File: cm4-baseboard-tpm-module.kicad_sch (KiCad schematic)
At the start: 37 parts, among them J1 Plug_Samtec_ERM5_2x20_ERM5-02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, U1 SLB9672XU20FW1624XTMA1

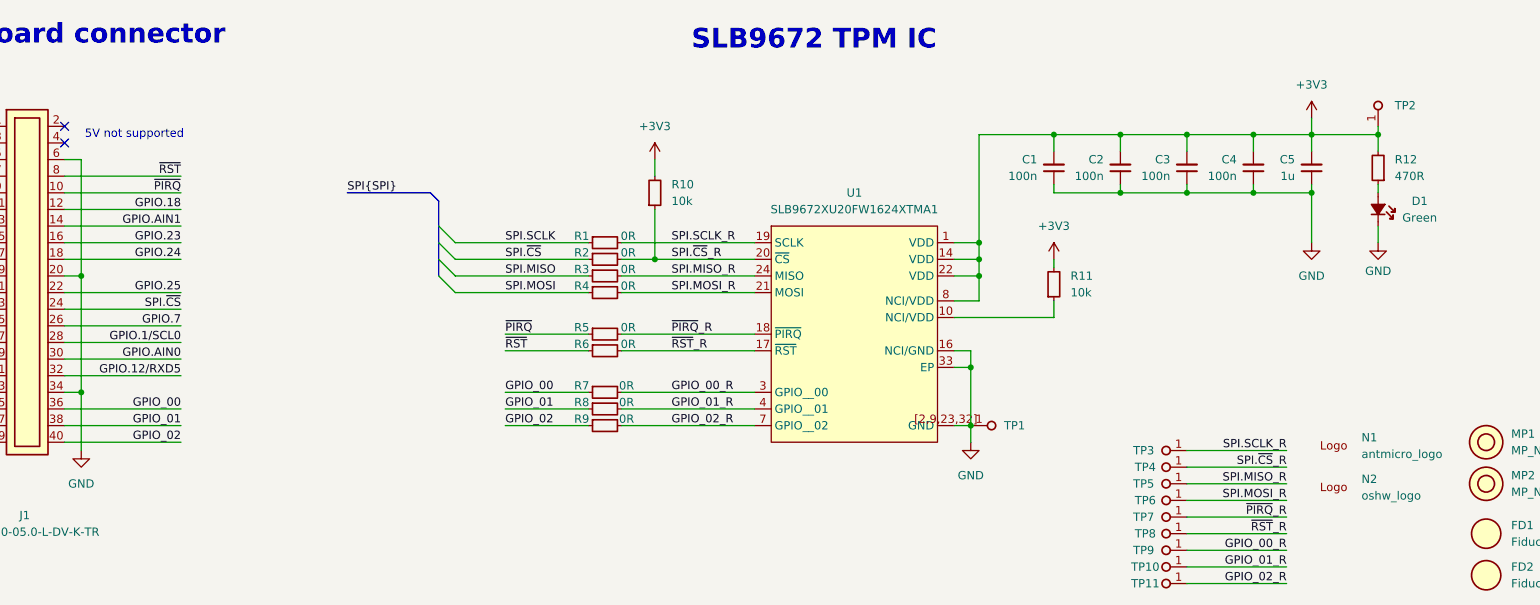
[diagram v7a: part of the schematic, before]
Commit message: [#104798] Create 2-layer board version
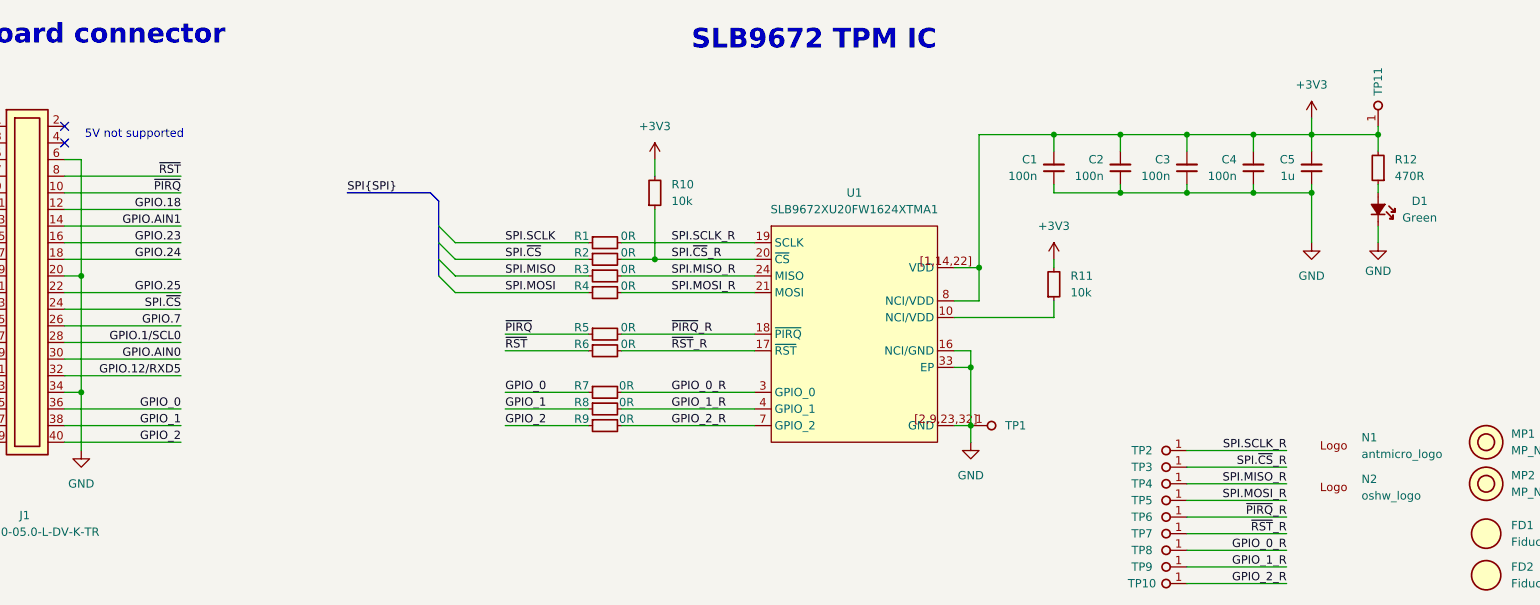
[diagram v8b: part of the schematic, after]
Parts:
- removed TP1, TP10, TP11, TP2, TP3, TP4, TP5, TP6, TP7, TP8, TP9: TP_Pad0.75mm_Drill0.2mm, antmicro-footprints:TP_Pad0.75mm_Drill0.2mm, symbol antmicroTestPoints:TP_Pad0.75mm_Drill0.2mm
- added TP1, TP10, TP11, TP2, TP3, TP4, TP5, TP6, TP7, TP8, TP9: TP_0.75mm_SMD, antmicro-footprints:TP_SMD_0.75mm, symbol antmicroTestPoints:TP_0.75mm_SMD
- U1: footprint antmicro-footprints:QFN-32-1EP_5x5mm_P0.5mm -> antmicro-footprints:UQFN-32-1EP_5x5mm_P0.5mm_EP3.6x3.6mm; License (none) -> Apache-2.0
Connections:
- net +3V3: now also U1.[1,14,22] (VDD), TP11.1; no longer U1.1 (VDD), U1.14 (VDD), U1.22 (VDD)
- net GND: now also TP1.1
- net SPI.MISO_R: now also TP4.1
- net SPI.MOSI_R: now also TP5.1
- net SPI.SCLK_R: now also TP2.1
- net SPI.~{CS}_R: now also TP3.1
- net ~{PIRQ}_R: now also TP6.1
- net ~{RST}_R: now also TP7.1
- net GPIO_00 renamed GPIO_0
- net GPIO_00_R renamed GPIO_0_R
- net GPIO_0_R: now also TP8.1
- net GPIO_01 renamed GPIO_1
- net GPIO_01_R renamed GPIO_1_R
- net GPIO_1_R: now also TP9.1
- net GPIO_02 renamed GPIO_2
- net GPIO_02_R renamed GPIO_2_R
- net GPIO_2_R: now also TP10.1
